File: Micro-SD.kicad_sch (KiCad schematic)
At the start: 8 parts, among them J502 503398-1892, Q501 IRLML6402

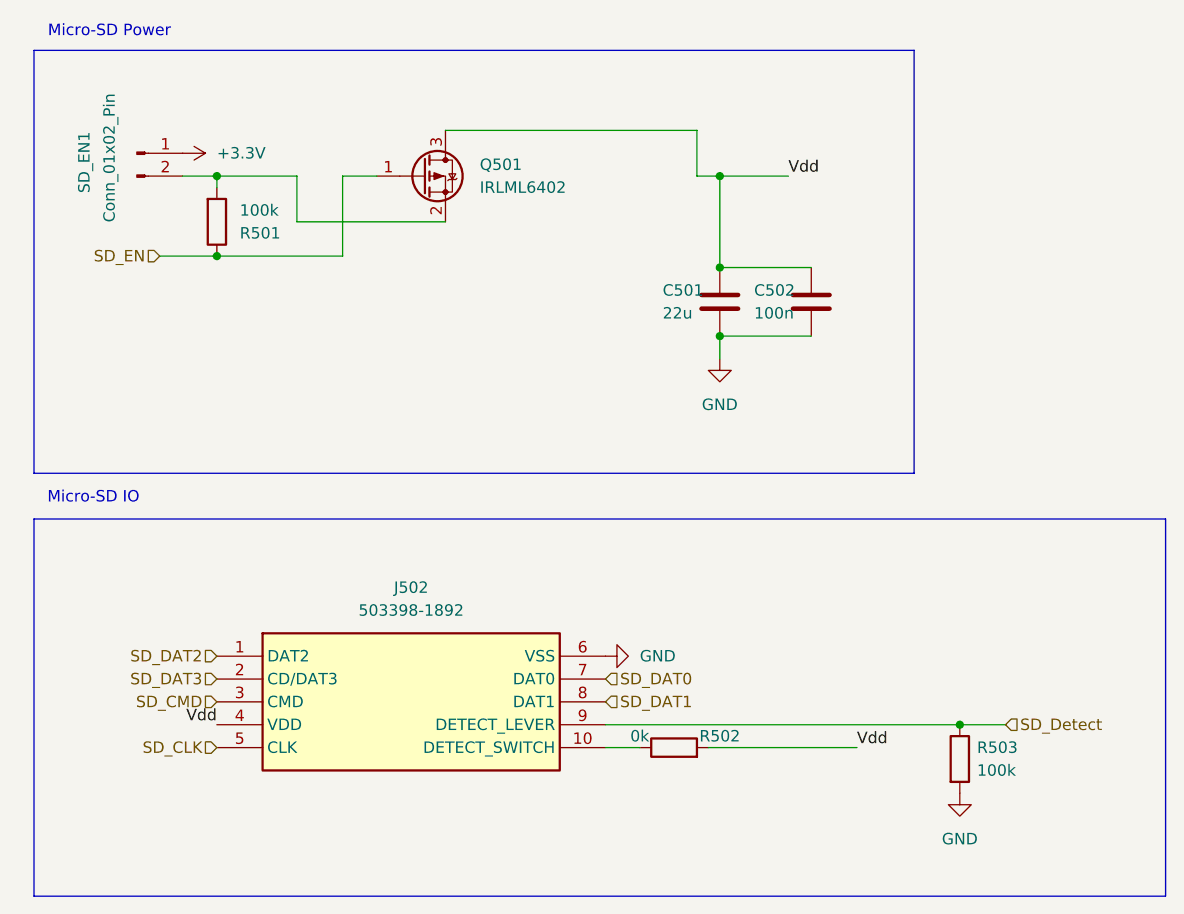
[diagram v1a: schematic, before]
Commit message: new layout
- recreation of the layout
- changed connection of ADC to MCU
- cleaner layout
- battery (supercap) for rtc
- crystal nearby the mcu
- 3V3 layer can be switched on/off separated from the mcu
- diode replaced with MOSFET
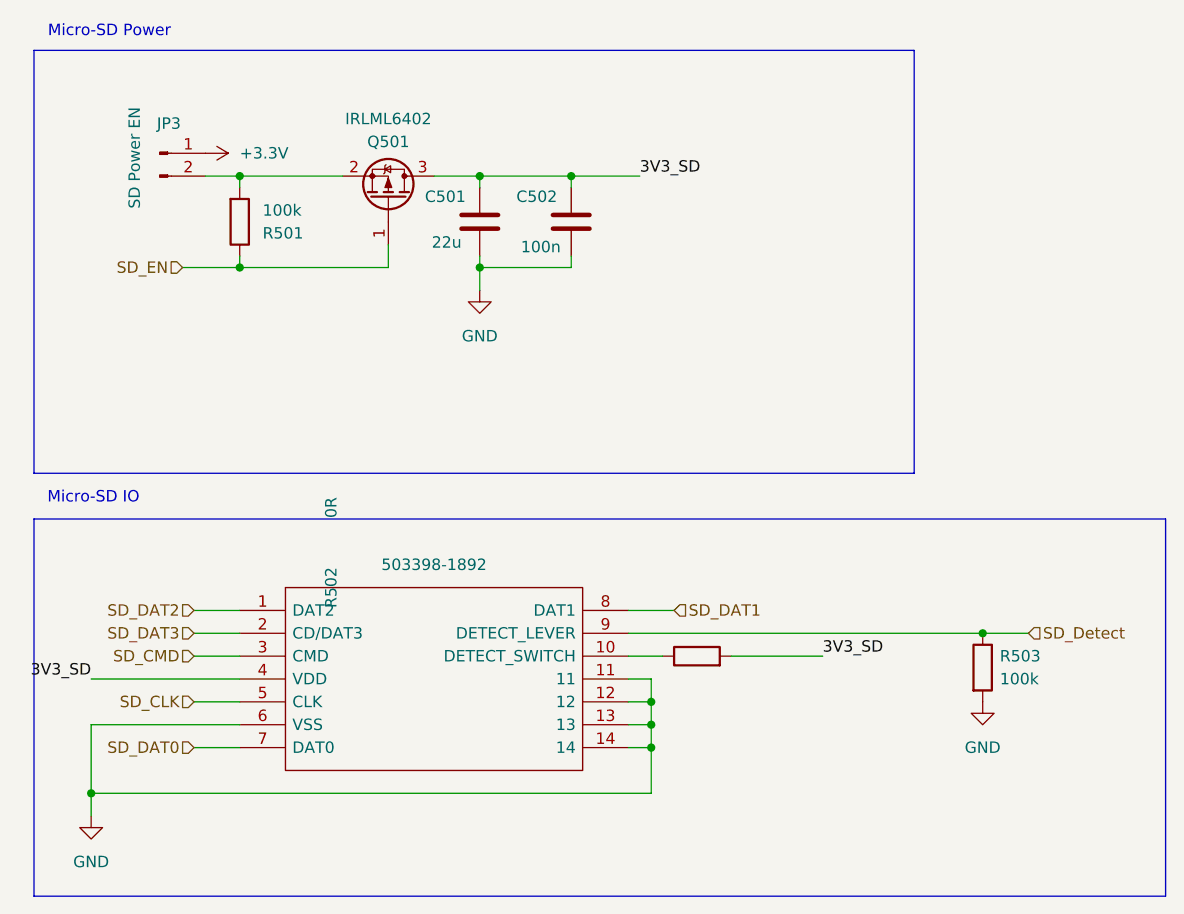
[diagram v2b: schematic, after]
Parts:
- removed J502: 503398-1892, Micro-SD:503398-1892-1, symbol molex Micro SD Verbinder:503398-1892
- added J502: 503398-1892, Bibliothek:503398-1892-1, symbol Connector:503398-1892
- C502: Mouser Part Number 187-CL21A226KQCLRNC -> 603-CC805KRX7R9BB104
- JP3: renamed from SD_EN1; Mouser Part Number (none) -> 523-G800NA306018EU
- Q501: Mouser Part Number (none) -> 942-IRLML6402TRPBF
- R502: value 0k -> 0R
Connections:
- net GND: now also J502.11, J502.12, J502.13, J502.14, J502.6 (VSS)
- net SD_CLK: now also J502.5 (CLK)
- net SD_CMD: now also J502.3 (CMD)
- net SD_DAT0: now also J502.7 (DAT0)
- net SD_DAT1: now also J502.8 (DAT1)
- net SD_DAT2: now also J502.1 (DAT2)
- net SD_DAT3: now also J502.2 (CD/DAT3)
- net SD_Detect: now also J502.9 (DETECT_LEVER)
- net at R502.1: now also J502.10 (DETECT_SWITCH)
- net Vdd renamed 3V3_SD
- net 3V3_SD: now also J502.4 (VDD)
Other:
- moved on the sheet: C501, C502, JP3, Q501, R501, R502, R503
